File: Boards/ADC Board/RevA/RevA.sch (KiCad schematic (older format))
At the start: 3 parts, among them M2.5 CMH

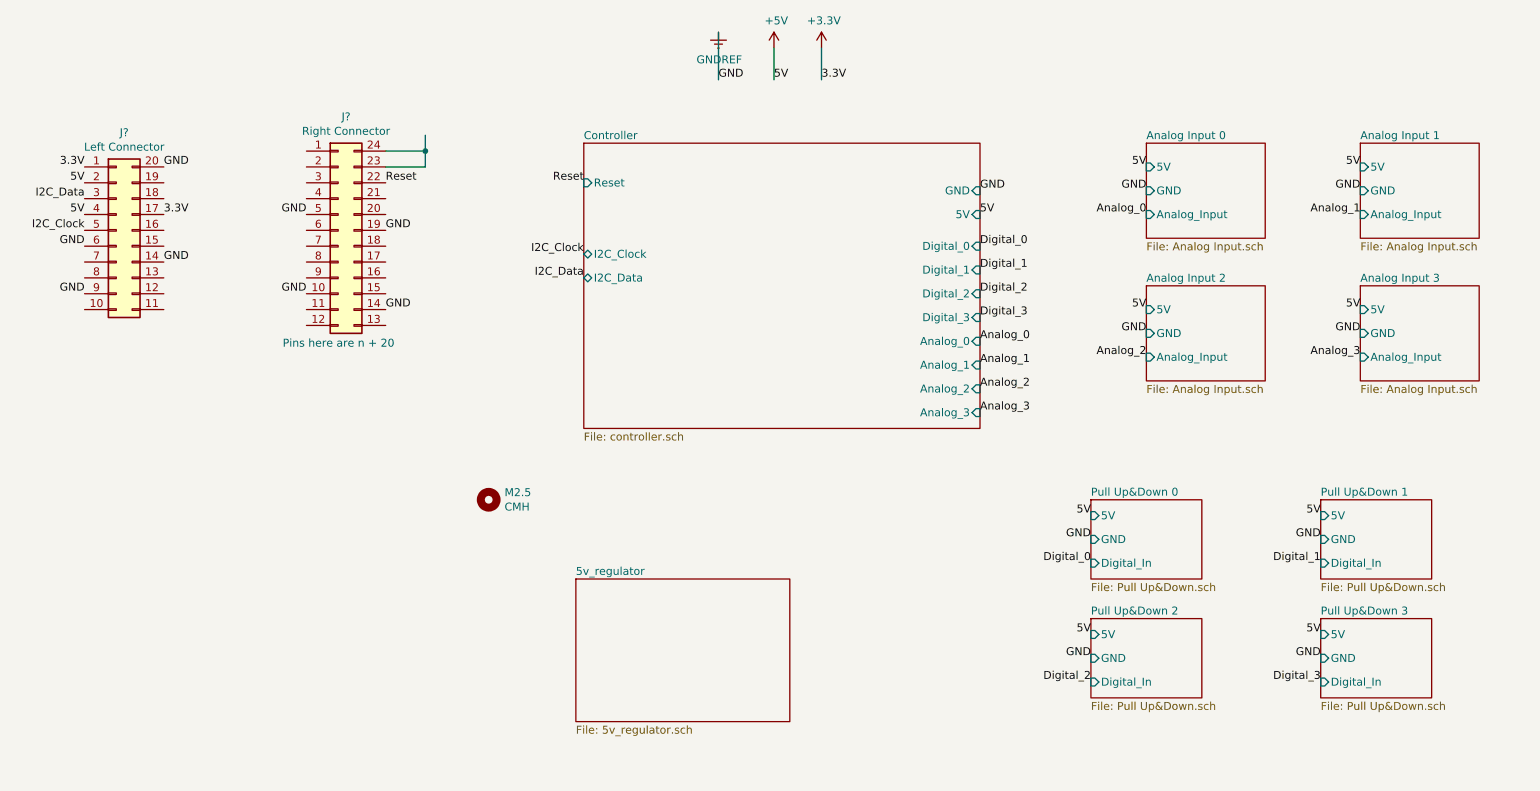
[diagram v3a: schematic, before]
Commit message: Connected power regulator to ADC and micro boards. Added no connects to headers on ADC board. Preformed some footprinting operations on ADC board.
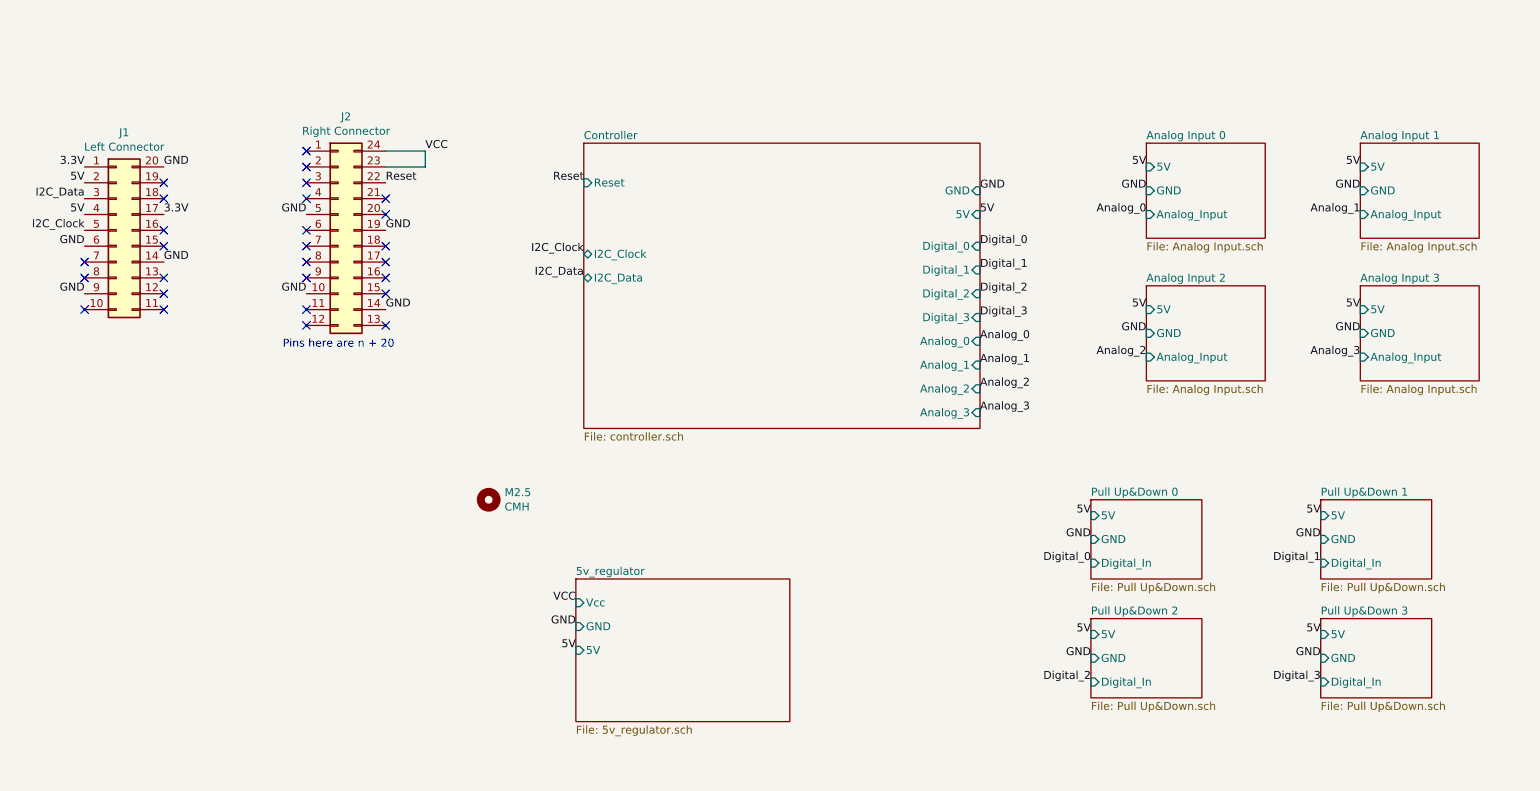
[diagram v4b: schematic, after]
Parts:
- gave numbers to parts that had none: 2
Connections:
- net labels added: VCC
- net labels removed: +3.3V, +5V, GNDREF
- wire segments 7 -> 3
- no-connect marks 0 -> 27
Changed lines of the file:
@@
 Text Label 7050 1750 0    50   ~ 0
 5V
-Text Label 5400 900  0    50   ~ 0
-GND
-Text Label 5750 900  0    50   ~ 0
-5V
-$Comp
-L power:+5V #PWR?
-U 1 1 6158EB64
-P 5750 700
-F 0 "#PWR?" H 5750 550 50  0001 C CNN
-F 1 "+5V" H 5765 873 50  0000 C CNN
-F 2 "" H 5750 700 50  0001 C CNN
-F 3 "" H 5750 700 50  0001 C CNN
-	1    5750 700
-	1    0    0    -1
-$EndComp
-Wire Wire Line
-	5750 700  5750 900
-$Comp
-L power:GNDREF #PWR?
-U 1 1 6158F66D
-P 5400 600
-F 0 "#PWR?" H 5400 350 50  0001 C CNN
-F 1 "GNDREF" H 5405 427 50  0000 C CNN
-F 2 "" H 5400 600 50  0001 C CNN
-F 3 "" H 5400 600 50  0001 C CNN
-	1    5400 600
-	1    0    0    -1
-$EndComp
-Wire Wire Line
-	5400 600  5400 900
-Text Label 6050 900  0    50   ~ 0
-3.3V
-$Comp
-L power:+3.3V #PWR?
-U 1 1 615902F5
-P 6050 700
-F 0 "#PWR?" H 6050 550 50  0001 C CNN
-F 1 "+3.3V" H 6065 873 50  0000 C CNN
-F 2 "" H 6050 700 50  0001 C CNN
-F 3 "" H 6050 700 50  0001 C CNN
-	1    6050 700
-	1    0    0    -1
-$EndComp
-Wire Wire Line
-	6050 700  6050 900
 $Sheet
 S 7750 3550 700  500
@@
 $EndSheet
 $Comp
-L Connector_Generic:Conn_02x10_Counter_Clockwise J?
+L Connector_Generic:Conn_02x10_Counter_Clockwise J1
 U 1 1 615E5E26
 P 1600 1850
-F 0 "J?" H 1650 2467 50  0000 C CNN
+F 0 "J1" H 1650 2467 50  0000 C CNN
 F 1 "Left Connector" H 1650 2376 50  0000 C CNN
 F 2 "" H 1600 1850 50  0001 C CNN
@@
 $EndComp
 $Comp
-L Connector_Generic:Conn_02x12_Counter_Clockwise J?
+L Connector_Generic:Conn_02x12_Counter_Clockwise J2
 U 1 1 615E7214
 P 3000 1850
-F 0 "J?" H 3050 2567 50  0000 C CNN
+F 0 "J2" H 3050 2567 50  0000 C CNN
 F 1 "Right Connector" H 3050 2476 50  0000 C CNN
 F 2 "" H 3000 1850 50  0001 C CNN
@@
 GND
 Wire Wire Line
-	3550 1350 3550 1250
-Wire Wire Line
 	3300 1350 3550 1350
 Wire Wire Line
@@
 Wire Wire Line
 	3550 1450 3300 1450
-Connection ~ 3550 1350
 Text Notes 2650 2600 0    50   ~ 0
 Pins here are n + 20
@@
 F0 "5v_regulator" 50
 F1 "5v_regulator.sch" 50
-$EndSheet
+F2 "Vcc" I L 4500 4200 50
+F3 "GND" I L 4500 4350 50
+F4 "5V" I L 4500 4500 50
+$EndSheet
+Text Label 4500 4200 2    50   ~ 0
+VCC
+Text Label 4500 4500 2    50   ~ 0
+5V
+Text Label 4500 4350 2    50   ~ 0
+GND
+Text Label 3550 1350 0    50   ~ 0
+VCC
+NoConn ~ 1900 1550
+NoConn ~ 1900 1650
+NoConn ~ 1900 1850
+NoConn ~ 1900 1950
+NoConn ~ 1400 2050
+NoConn ~ 1400 2150
+NoConn ~ 1400 2350
+NoConn ~ 1900 2350
+NoConn ~ 1900 2250
+NoConn ~ 1900 2150
+NoConn ~ 2800 2450
+NoConn ~ 2800 2350
+NoConn ~ 2800 2150
+NoConn ~ 2800 2050
+NoConn ~ 2800 1950
+NoConn ~ 2800 1850
+NoConn ~ 2800 1650
+NoConn ~ 2800 1550
+NoConn ~ 2800 1450
+NoConn ~ 2800 1350
+NoConn ~ 3300 1650
+NoConn ~ 3300 1750
+NoConn ~ 3300 1950
+NoConn ~ 3300 2050
+NoConn ~ 3300 2150
+NoConn ~ 3300 2250
+NoConn ~ 3300 2450
 $EndSCHEMATC

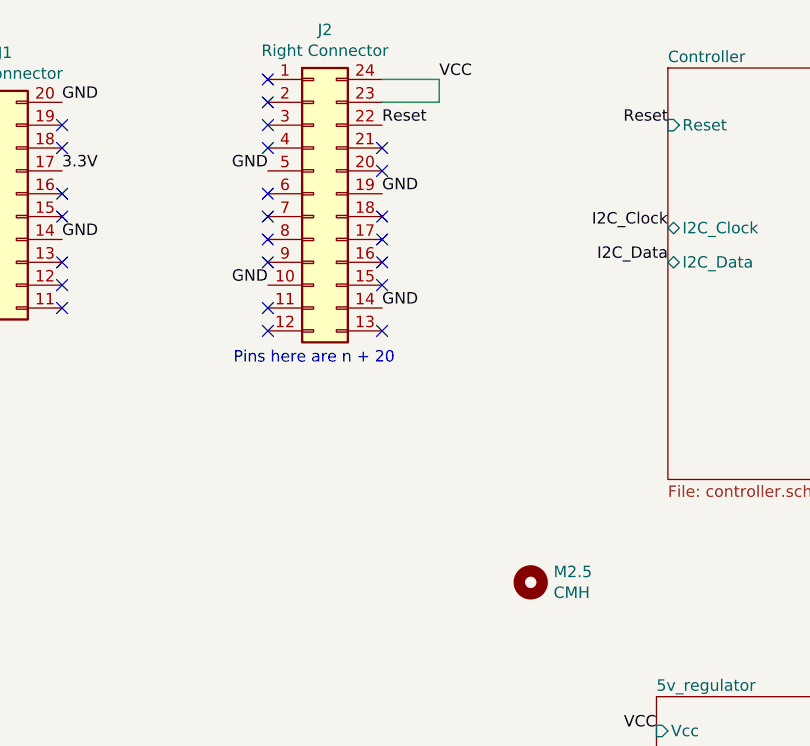
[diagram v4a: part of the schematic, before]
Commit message: Fixed regulator nonsense on ADC board. Rules checked both ADC and micro boards. Fixed interconnect on ADC board.
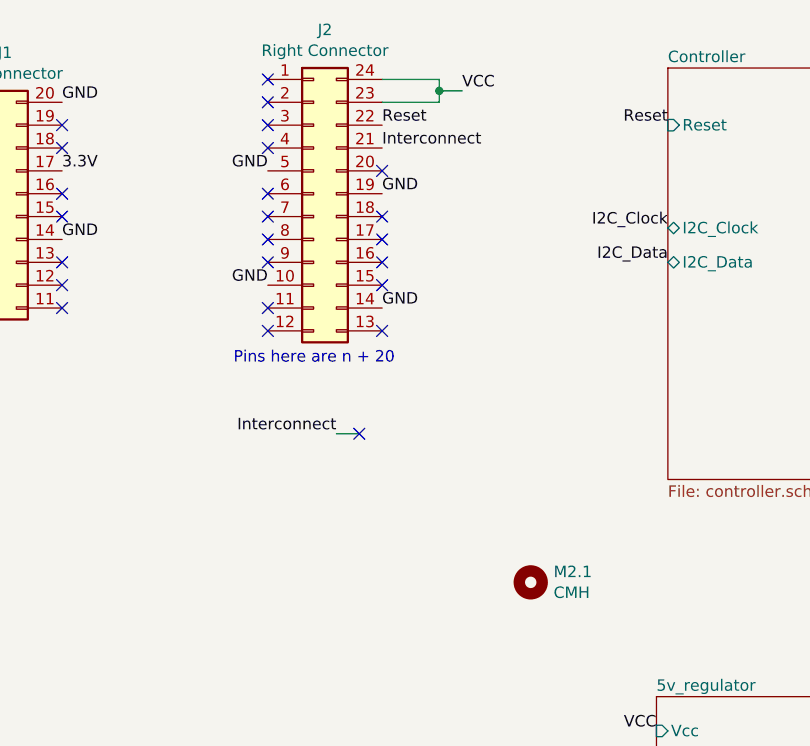
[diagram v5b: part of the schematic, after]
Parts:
- renumbered M2.5 to M2.1
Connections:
- net Interconnect: now reaches J2.21 (Pin_21)
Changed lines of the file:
@@
 	3300 1350 3550 1350
 Wire Wire Line
-	3550 1350 3550 1450
+	3550 1350 3550 1400
 Wire Wire Line
 	3550 1450 3300 1450
@@
 I2C_Clock
 $Comp
-L Mechanical:MountingHole M2.5
+L Mechanical:MountingHole M2.1
 U 1 1 616626E5
 P 3950 3550
-F 0 "M2.5" H 4050 3596 50  0000 L CNN
+F 0 "M2.1" H 4050 3596 50  0000 L CNN
 F 1 "CMH" H 4050 3505 50  0000 L CNN
 F 2 "" H 3950 3550 50  0001 C CNN
@@
 Text Label 4500 4350 2    50   ~ 0
 GND
-Text Label 3550 1350 0    50   ~ 0
+Text Label 3650 1400 0    50   ~ 0
 VCC
 NoConn ~ 1900 1550
@@
 NoConn ~ 2800 1450
 NoConn ~ 2800 1350
-NoConn ~ 3300 1650
 NoConn ~ 3300 1750
 NoConn ~ 3300 1950
@@
 NoConn ~ 3300 2250
 NoConn ~ 3300 2450
+Wire Wire Line
+	3650 1400 3550 1400
+Connection ~ 3550 1400
+Wire Wire Line
+	3550 1400 3550 1450
+Text Label 3300 1650 0    50   ~ 0
+Interconnect
+Text Label 3100 2900 2    50   ~ 0
+Interconnect
+Wire Wire Line
+	3100 2900 3200 2900
+NoConn ~ 3200 2900
 $EndSCHEMATC

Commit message: Began PCB layout for ADC board. Fixed annotations for ADC and micro boards.
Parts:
- J1: footprint (none) -> Connector_PinHeader_2.54mm:PinHeader_1x10_P2.54mm_Vertical
- J2: footprint (none) -> Connector_PinHeader_2.54mm:PinHeader_1x12_P2.54mm_Vertical
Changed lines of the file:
@@
 F 0 "J1" H 1650 2467 50  0000 C CNN
 F 1 "Left Connector" H 1650 2376 50  0000 C CNN
-F 2 "" H 1600 1850 50  0001 C CNN
+F 2 "Connector_PinHeader_2.54mm:PinHeader_1x10_P2.54mm_Vertical" H 1600 1850 50  0001 C CNN
 F 3 "~" H 1600 1850 50  0001 C CNN
 	1    1600 1850
@@
 F 0 "J2" H 3050 2567 50  0000 C CNN
 F 1 "Right Connector" H 3050 2476 50  0000 C CNN
-F 2 "" H 3000 1850 50  0001 C CNN
+F 2 "Connector_PinHeader_2.54mm:PinHeader_1x12_P2.54mm_Vertical" H 3000 1850 50  0001 C CNN
 F 3 "~" H 3000 1850 50  0001 C CNN
 	1    3000 1850

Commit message: Completed footprint associations for ADC board. Generated netlist for ADC board. Started PCB design for ADC board.
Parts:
- M2.1: footprint (none) -> MountingHole:MountingHole_2.7mm_M2.5
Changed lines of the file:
@@
 F 0 "M2.1" H 4050 3596 50  0000 L CNN
 F 1 "CMH" H 4050 3505 50  0000 L CNN
-F 2 "" H 3950 3550 50  0001 C CNN
+F 2 "MountingHole:MountingHole_2.7mm_M2.5" H 3950 3550 50  0001 C CNN
 F 3 "~" H 3950 3550 50  0001 C CNN
 	1    3950 3550
